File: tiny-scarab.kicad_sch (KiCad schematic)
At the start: 40 parts, among them J3 Conn_02x07_Odd_Even, J4 Conn_02x07_Odd_Even, J5 Screw_Hole, J6 Screw_Hole, J7 Screw_Hole, J8 Screw_Hole

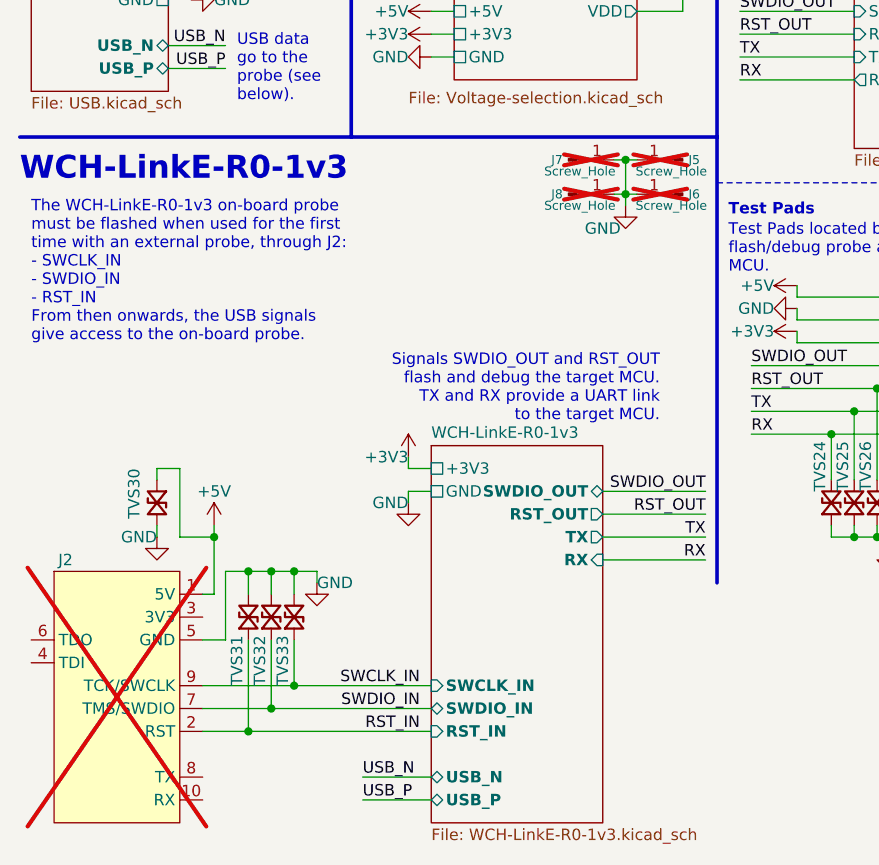
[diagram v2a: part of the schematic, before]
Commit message: Prefix each symbol name in library - eg. 'D_', 'CONN_', 'IC_', ...
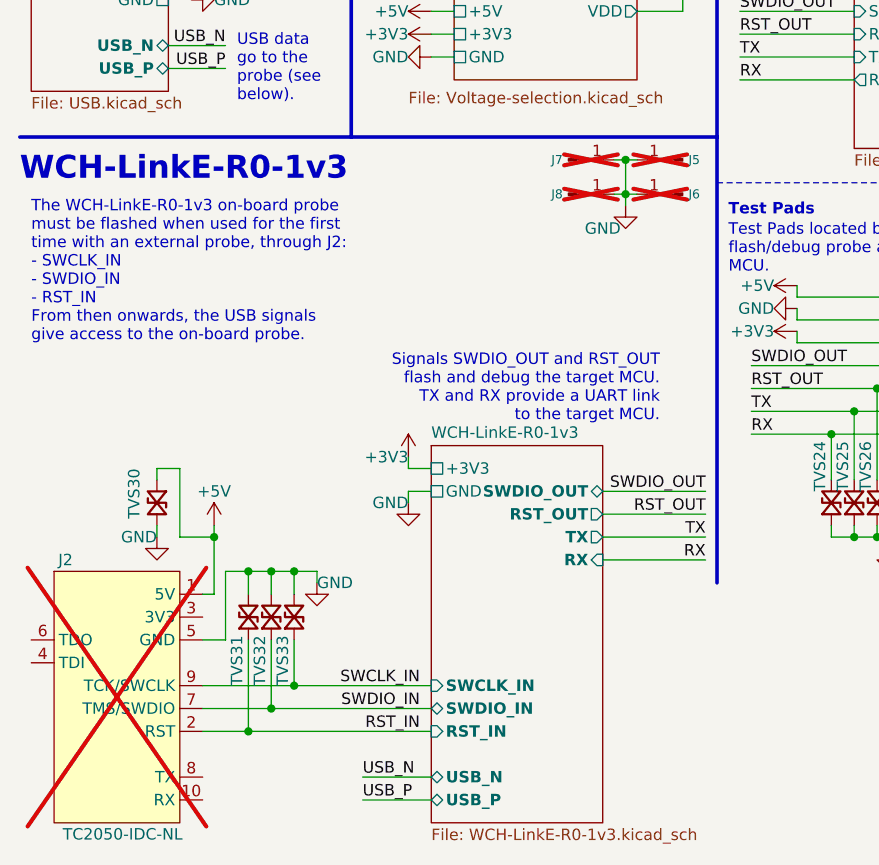
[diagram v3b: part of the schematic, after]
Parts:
- J2: value ~ -> TC2050-IDC-NL; symbol Tiny_Scarab:TC2050-IDC-NL-WCH-LinkE-R0-1v3 -> Tiny_Scarab:CONN_TC2050-IDC-NL; SPN TC2050-IDC-NL-ND -> (none); Supplier DigiKey -> (none)
- J3, J4: value Conn_02x07_Odd_Even -> CONN_PIN_HEADER_02x07; symbol Tiny_Scarab:Conn_02x07_Odd_Even -> Tiny_Scarab:CONN_PIN_HEADER_02x07; SPN 10129383-914001ALF-ND -> (none); Supplier DigiKey -> (none)
- J5, J6, J7, J8: value Screw_Hole -> 3mm; symbol Tiny_Scarab:Screw_Hole -> Tiny_Scarab:SCREW_HOLE
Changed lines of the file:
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@@
     )
   )
-  (symbol (lib_id "Tiny_Scarab:Screw_Hole") (at 86.36 57.15 0) (mirror y) (unit 1)
+  (symbol (lib_id "Tiny_Scarab:SCREW_HOLE") (at 86.36 57.15 0) (mirror y) (unit 1)
     (in_bom no) (on_board yes) (dnp yes)
     (property "Reference" "J5" (at 87.63 57.15 0)
       (effects (font (size 1 1)))
     )
-    (property "Value" "Screw_Hole" (at 85.09 58.42 0)
-      (effects (font (size 1 1)))
-    )
-    (property "Footprint" "Tiny_Scarab:Screw_Hole" (at 86.36 49.53 0)
-      (effects (font (size 1.27 1.27)) hide)
-    )
-    (property "Datasheet" "~" (at 86.36 52.07 0)
+    (property "Value" "3mm" (at 91.44 57.15 0)
+      (effects (font (size 1.27 1.27)) hide)
+    )
+    (property "Footprint" "Tiny_Scarab:Screw_Hole" (at 86.36 52.07 0)
+      (effects (font (size 1.27 1.27)) hide)
+    )
+    (property "Datasheet" "" (at 86.36 52.07 0)
       (effects (font (size 1.27 1.27)) hide)
     )
@@
     )
   )
-  (symbol (lib_id "Tiny_Scarab:Screw_Hole") (at 86.36 60.96 0) (mirror y) (unit 1)
+  (symbol (lib_id "Tiny_Scarab:SCREW_HOLE") (at 86.36 60.96 0) (mirror y) (unit 1)
     (in_bom no) (on_board yes) (dnp yes)
     (property "Reference" "J6" (at 87.63 60.96 0)
       (effects (font (size 1 1)))
     )
-    (property "Value" "Screw_Hole" (at 85.09 62.23 0)
-      (effects (font (size 1 1)))
-    )
-    (property "Footprint" "Tiny_Scarab:Screw_Hole" (at 86.36 53.34 0)
-      (effects (font (size 1.27 1.27)) hide)
-    )
-    (property "Datasheet" "~" (at 86.36 55.88 0)
+    (property "Value" "3mm" (at 86.36 63.5 0)
+      (effects (font (size 1.27 1.27)) hide)
+    )
+    (property "Footprint" "Tiny_Scarab:Screw_Hole" (at 86.36 55.88 0)
+      (effects (font (size 1.27 1.27)) hide)
+    )
+    (property "Datasheet" "" (at 86.36 55.88 0)
       (effects (font (size 1.27 1.27)) hide)
     )
@@
     )
   )
-  (symbol (lib_id "Tiny_Scarab:Conn_02x07_Odd_Even") (at 166.37 64.77 0) (unit 1)
+  (symbol (lib_id "Tiny_Scarab:CONN_PIN_HEADER_02x07") (at 166.37 64.77 0) (unit 1)
     (in_bom yes) (on_board yes) (dnp no)
     (property "Reference" "J4" (at 166.37 54.61 0)
       (effects (font (size 1.27 1.27)))
     )
-    (property "Value" "Conn_02x07_Odd_Even" (at 167.64 53.34 0)
-      (effects (font (size 1.27 1.27)) hide)
-    )
-    (property "Footprint" "Tiny_Scarab:PinHeader_2x07_P2.54mm_Vertical_SMD_10129383-914001ALF" (at 167.64 31.75 0)
-      (effects (font (size 1.27 1.27)) hide)
-    )
-    (property "Datasheet" "https://cdn.amphenol-cs.com/media/wysiwyg/files/drawing/10129383.pdf" (at 165.1 34.29 0)
-      (effects (font (size 1.27 1.27)) hide)
-    )
-    (property "Manufacturer" "BOOMELE(Boom Precision Elec)" (at 166.37 36.83 0)
-      (effects (font (size 1.27 1.27)) hide)
-    )
-    (property "MPN" "C84004" (at 166.37 39.37 0)
-      (effects (font (size 1.27 1.27)) hide)
-    )
-    (property "JLCPCB Part #" "C84004" (at 166.37 44.45 0)
-      (effects (font (size 1.27 1.27)) hide)
-    )
-    (property "Supplier" "DigiKey" (at 166.37 41.91 0)
-      (effects (font (size 1.27 1.27)) hide)
-    )
-    (property "SPN" "10129383-914001ALF-ND" (at 166.37 44.45 0)
+    (property "Value" "CONN_PIN_HEADER_02x07" (at 167.64 53.34 0)
+      (effects (font (size 1.27 1.27)) hide)
+    )
+    (property "Footprint" "Tiny_Scarab:PinHeader_2x07_P2.54mm_Vertical_SMD_10129383-914001ALF" (at 167.64 43.18 0)
+      (effects (font (size 1.27 1.27)) hide)
+    )
+    (property "Datasheet" "" (at 165.1 43.18 0)
+      (effects (font (size 1.27 1.27)) hide)
+    )
+    (property "Manufacturer" "BOOMELE(Boom Precision Elec)" (at 166.37 45.72 0)
+      (effects (font (size 1.27 1.27)) hide)
+    )
+    (property "MPN" "C84004" (at 166.37 48.26 0)
+      (effects (font (size 1.27 1.27)) hide)
+    )
+    (property "JLCPCB Part #" "C84004" (at 166.37 50.8 0)
       (effects (font (size 1.27 1.27)) hide)
     )
     (property "DigiKey" "" (at 166.37 64.77 0)
-      (effects (font (size 1.27 1.27)))
+      (effects (font (size 1.27 1.27)) hide)
     )
     (property "Farnell" "" (at 166.37 64.77 0)
-      (effects (font (size 1.27 1.27)))
+      (effects (font (size 1.27 1.27)) hide)
     )
     (property "Mouser" "" (at 166.37 64.77 0)
-      (effects (font (size 1.27 1.27)))
+      (effects (font (size 1.27 1.27)) hide)
     )
     (pin "6")
@@
     )
   )
-  (symbol (lib_id "Tiny_Scarab:Screw_Hole") (at 73.66 57.15 0) (unit 1)
+  (symbol (lib_id "Tiny_Scarab:SCREW_HOLE") (at 73.66 57.15 0) (unit 1)
     (in_bom no) (on_board yes) (dnp yes)
     (property "Reference" "J7" (at 72.39 57.15 0)
       (effects (font (size 1 1)))
     )
-    (property "Value" "Screw_Hole" (at 74.93 58.42 0)
-      (effects (font (size 1 1)))
-    )
-    (property "Footprint" "Tiny_Scarab:Screw_Hole" (at 73.66 49.53 0)
-      (effects (font (size 1.27 1.27)) hide)
-    )
-    (property "Datasheet" "~" (at 73.66 52.07 0)
+    (property "Value" "3mm" (at 68.58 57.15 0)
+      (effects (font (size 1.27 1.27)) hide)
+    )
+    (property "Footprint" "Tiny_Scarab:Screw_Hole" (at 73.66 52.07 0)
+      (effects (font (size 1.27 1.27)) hide)
+    )
+    (property "Datasheet" "" (at 73.66 52.07 0)
       (effects (font (size 1.27 1.27)) hide)
     )
@@
     )
   )
-  (symbol (lib_id "Tiny_Scarab:Conn_02x07_Odd_Even") (at 166.37 40.64 0) (unit 1)
+  (symbol (lib_id "Tiny_Scarab:CONN_PIN_HEADER_02x07") (at 166.37 40.64 0) (unit 1)
     (in_bom yes) (on_board yes) (dnp no)
     (property "Reference" "J3" (at 166.37 30.48 0)
       (effects (font (size 1.27 1.27)))
     )
-    (property "Value" "Conn_02x07_Odd_Even" (at 167.64 29.21 0)
-      (effects (font (size 1.27 1.27)) hide)
-    )
-    (property "Footprint" "Tiny_Scarab:PinHeader_2x07_P2.54mm_Vertical_SMD_10129383-914001ALF" (at 167.64 7.62 0)
-      (effects (font (size 1.27 1.27)) hide)
-    )
-    (property "Datasheet" "https://cdn.amphenol-cs.com/media/wysiwyg/files/drawing/10129383.pdf" (at 165.1 10.16 0)
-      (effects (font (size 1.27 1.27)) hide)
-    )
-    (property "Manufacturer" "BOOMELE(Boom Precision Elec)" (at 166.37 12.7 0)
-      (effects (font (size 1.27 1.27)) hide)
-    )
-    (property "MPN" "C84004" (at 166.37 15.24 0)
-      (effects (font (size 1.27 1.27)) hide)
-    )
-    (property "JLCPCB Part #" "C84004" (at 166.37 40.64 0)
-      (effects (font (size 1.27 1.27)) hide)
-    )
-    (property "Supplier" "DigiKey" (at 166.37 17.78 0)
-      (effects (font (size 1.27 1.27)) hide)
-    )
-    (property "SPN" "10129383-914001ALF-ND" (at 166.37 20.32 0)
+    (property "Value" "CONN_PIN_HEADER_02x07" (at 167.64 29.21 0)
+      (effects (font (size 1.27 1.27)) hide)
+    )
+    (property "Footprint" "Tiny_Scarab:PinHeader_2x07_P2.54mm_Vertical_SMD_10129383-914001ALF" (at 167.64 19.05 0)
+      (effects (font (size 1.27 1.27)) hide)
+    )
+    (property "Datasheet" "" (at 165.1 19.05 0)
+      (effects (font (size 1.27 1.27)) hide)
+    )
+    (property "Manufacturer" "BOOMELE(Boom Precision Elec)" (at 166.37 21.59 0)
+      (effects (font (size 1.27 1.27)) hide)
+    )
+    (property "MPN" "C84004" (at 166.37 24.13 0)
+      (effects (font (size 1.27 1.27)) hide)
+    )
+    (property "JLCPCB Part #" "C84004" (at 166.37 26.67 0)
       (effects (font (size 1.27 1.27)) hide)
     )
     (property "DigiKey" "" (at 166.37 40.64 0)
-      (effects (font (size 1.27 1.27)))
+      (effects (font (size 1.27 1.27)) hide)
     )
     (property "Farnell" "" (at 166.37 40.64 0)
-      (effects (font (size 1.27 1.27)))
+      (effects (font (size 1.27 1.27)) hide)
     )
     (property "Mouser" "" (at 166.37 40.64 0)
-      (effects (font (size 1.27 1.27)))
+      (effects (font (size 1.27 1.27)) hide)
     )
     (pin "6")
@@
     )
   )
-  (symbol (lib_id "Tiny_Scarab:TC2050-IDC-NL-WCH-LinkE-R0-1v3") (at 22.86 116.84 0) (unit 1)
+  (symbol (lib_id "Tiny_Scarab:CONN_TC2050-IDC-NL") (at 22.86 116.84 0) (unit 1)
     (in_bom no) (on_board yes) (dnp yes)
     (property "Reference" "J2" (at 17.78 101.6 0)
       (effects (font (size 1.27 1.27)))
     )
-    (property "Value" "~" (at 20.32 116.84 0)
+    (property "Value" "TC2050-IDC-NL" (at 24.13 132.08 0)
       (effects (font (size 1.27 1.27)))
     )
@@
     )
     (property "MPN" "TC2050-IDC-NL" (at 50.8 111.76 0)
-      (effects (font (size 1.27 1.27)) (justify left) hide)
-    )
-    (property "Supplier" "DigiKey" (at 50.8 114.3 0)
-      (effects (font (size 1.27 1.27)) (justify left) hide)
-    )
-    (property "SPN" "TC2050-IDC-NL-ND" (at 50.8 116.84 0)
       (effects (font (size 1.27 1.27)) (justify left) hide)
     )
@@
     )
   )
-  (symbol (lib_id "Tiny_Scarab:Screw_Hole") (at 73.66 60.96 0) (unit 1)
+  (symbol (lib_id "Tiny_Scarab:SCREW_HOLE") (at 73.66 60.96 0) (unit 1)
     (in_bom no) (on_board yes) (dnp yes)
     (property "Reference" "J8" (at 72.39 60.96 0)
       (effects (font (size 1 1)))
     )
-    (property "Value" "Screw_Hole" (at 74.93 62.23 0)
-      (effects (font (size 1 1)))
-    )
-    (property "Footprint" "Tiny_Scarab:Screw_Hole" (at 73.66 53.34 0)
-      (effects (font (size 1.27 1.27)) hide)
-    )
-    (property "Datasheet" "~" (at 73.66 55.88 0)
-      (effects (font (size 1.27 1.27)) hide)
-    )
+    (property "Value" "3mm" (at 68.58 60.96 0)
+      (effects (font (size 1.27 1.27)) hide)
+    )
+    (property "Footprint" "Tiny_Scarab:Screw_Hole" (at 73.66 55.88 0)
+      (effects (font (size 1.27 1.27)) hide)
+    )
+    (property "Datasheet" "" (at 73.66 55.88 0)
+      (effects (font (size 1.27 1.27)) hide)
+    )

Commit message: Delete unused footprints
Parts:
- J3, J4: footprint Tiny_Scarab:PinHeader_2x07_P2.54mm_Vertical_SMD_10129383-914001ALF -> Tiny_Scarab:CONN_PIN_HEADER_2x07_P2.54mm_Vertical_SMD
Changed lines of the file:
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@@
       (effects (font (size 1.27 1.27)) hide)
     )
-    (property "Footprint" "Tiny_Scarab:PinHeader_2x07_P2.54mm_Vertical_SMD_10129383-914001ALF" (at 167.64 43.18 0)
+    (property "Footprint" "Tiny_Scarab:CONN_PIN_HEADER_2x07_P2.54mm_Vertical_SMD" (at 167.64 43.18 0)
       (effects (font (size 1.27 1.27)) hide)
     )
@@
       (effects (font (size 1.27 1.27)) hide)
     )
-    (property "Footprint" "Tiny_Scarab:PinHeader_2x07_P2.54mm_Vertical_SMD_10129383-914001ALF" (at 167.64 19.05 0)
-      (effects (font (size 1.27 1.27)) hide)
-    )
+    (property "Footprint" "Tiny_Scarab:CONN_PIN_HEADER_2x07_P2.54mm_Vertical_SMD" (at 167.64 19.05 0)
+      (effects (font (size 1.27 1.27)) hide)
+    )
